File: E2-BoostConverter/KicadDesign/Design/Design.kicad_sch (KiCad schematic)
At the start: 16 parts, among them J1 Screw_Terminal_01x02, J2 Screw_Terminal_01x02, Q1 IRF740, U1 IR2110, U2 TL494, U4 LM7809CT

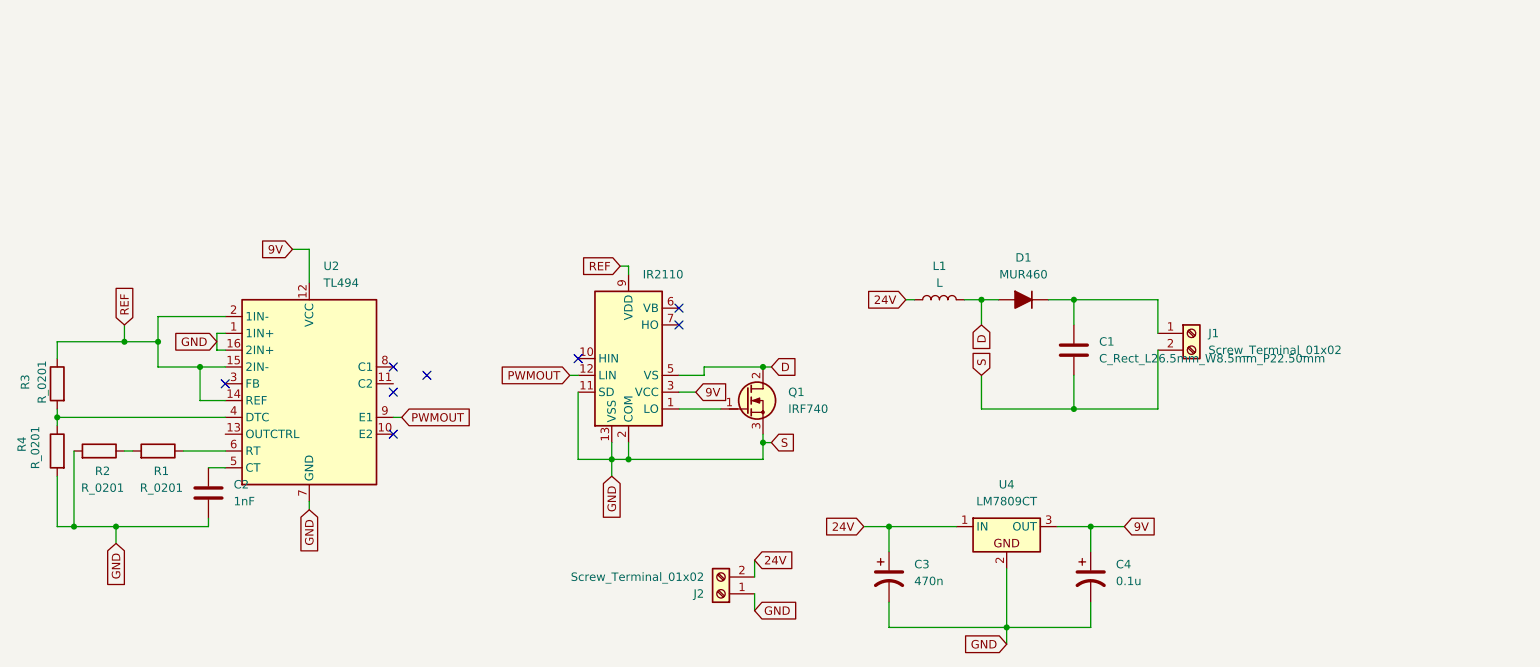
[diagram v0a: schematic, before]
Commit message: created E3-ACDC and updated E2-ClassD
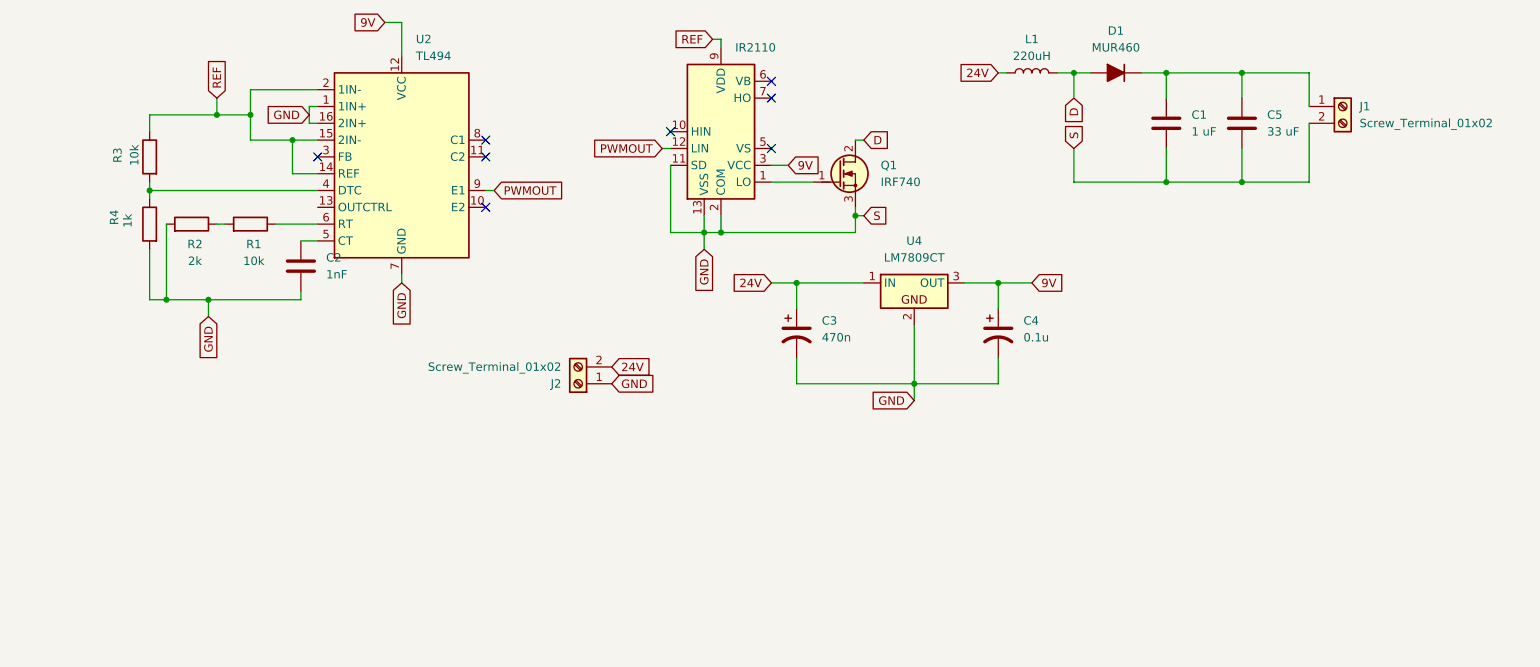
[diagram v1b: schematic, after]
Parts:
- added C5: 33 uF, PCM_Capacitor_THT_AKL:C_Rect_L26.5mm_W8.5mm_P22.50mm_MKS4, symbol PCM_Capacitor_AKL:C_Rect_L26.5mm_W8.5mm_P22.50mm
- C1: value C_Rect_L26.5mm_W8.5mm_P22.50mm -> 1 uF
- L1: value L -> 220uH
- R1, R3: value R_0201 -> 10k
- R2: value R_0201 -> 2k
- R4: value R_0201 -> 1k
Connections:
- net D: no longer U1.5 (VS)
- net GND: now also C5.2
- net at C1.1, D1.1 (K), J1.1 (Pin_1): now also C5.1
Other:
- moved on the sheet: C1, C2, C3, C4, D1, J1, J2, L1, Q1, R1, R2, R3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
